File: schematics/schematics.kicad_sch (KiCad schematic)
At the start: 6 parts, among them Q1 IRF9540N, U1 WeMos_D1_mini, U2 74AHC1G04

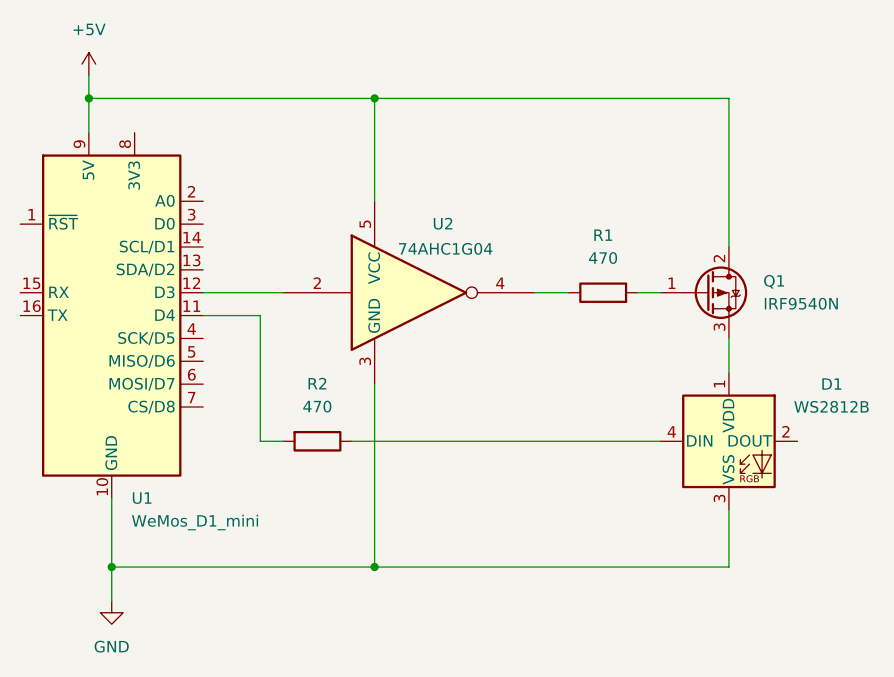
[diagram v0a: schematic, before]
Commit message: small p-MOS fuckup
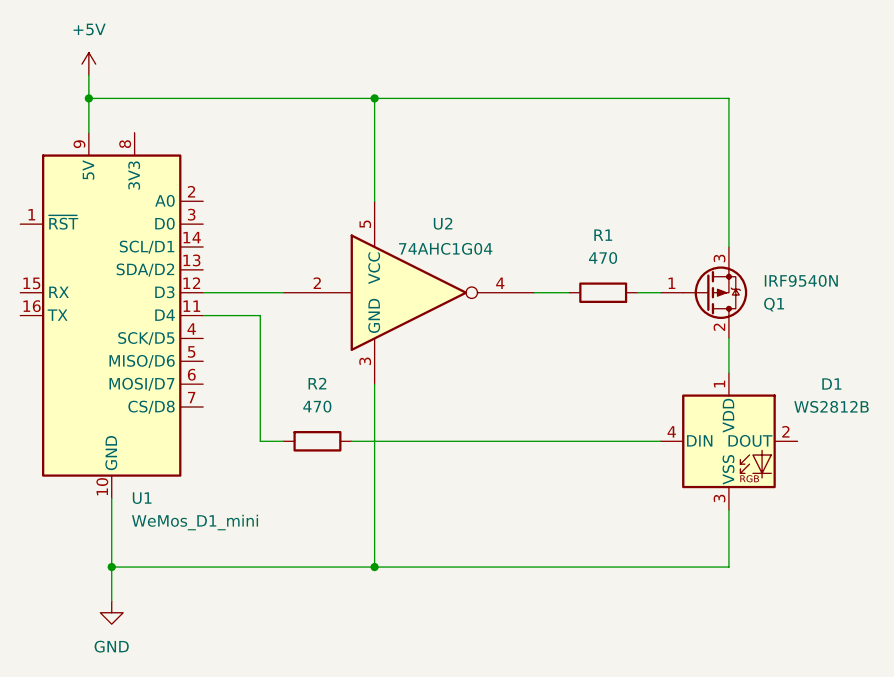
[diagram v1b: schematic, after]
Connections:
- net +5V: now also Q1.3 (S); no longer Q1.2 (D)
- net at D1.1 (VDD): now also Q1.2 (D); no longer Q1.3 (S)
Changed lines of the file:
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@@
 		(lib_id "Transistor_FET:IRF9540N")
 		(at 153.67 88.9 0)
+		(mirror x)
 		(unit 1)
 		(exclude_from_sim no)
@@
 		(on_board yes)
 		(dnp no)
-		(fields_autoplaced yes)
 		(property "Reference" "Q1"
-			(at 160.02 87.6299 0)
+			(at 160.02 90.1701 0)
 			(effects
 				(font
@@
 		)
 		(property "Value" "IRF9540N"
-			(at 160.02 90.1699 0)
+			(at 160.02 87.6301 0)
 			(effects
 				(font
@@
 		)
 		(property "Footprint" "Package_TO_SOT_THT:TO-220-3_Vertical"
-			(at 158.75 90.805 0)
+			(at 158.75 86.995 0)
 			(effects
 				(font
@@
 		)
 		(property "Datasheet" "http://www.irf.com/product-info/datasheets/data/irf9540n.pdf"
-			(at 158.75 92.71 0)
+			(at 158.75 85.09 0)
 			(effects
 				(font
